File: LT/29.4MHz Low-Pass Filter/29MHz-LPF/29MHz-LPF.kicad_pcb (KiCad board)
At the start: 2 copper layers, 71.8 x 19.7 mm, 12 parts, among them J1 Conn_Coaxial, J2 Conn_Coaxial

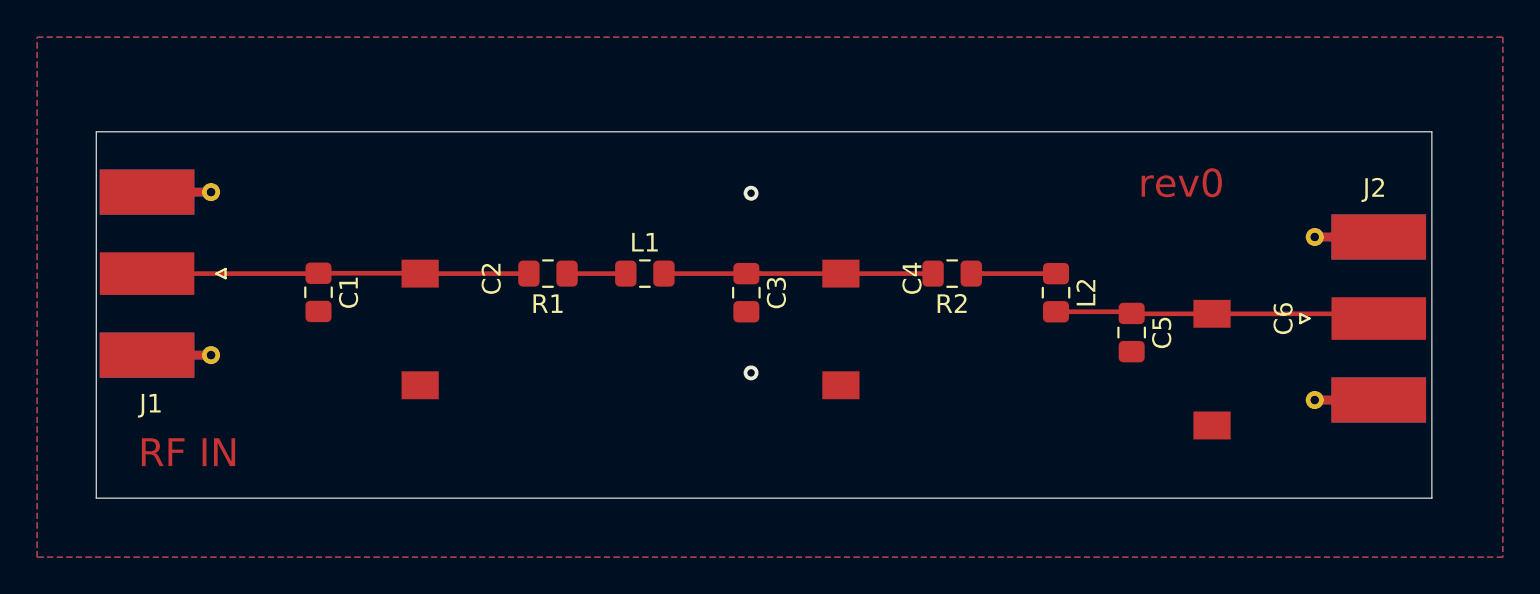
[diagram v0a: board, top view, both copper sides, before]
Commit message: removed 0 ohm resistors on 29.4MHz LPF
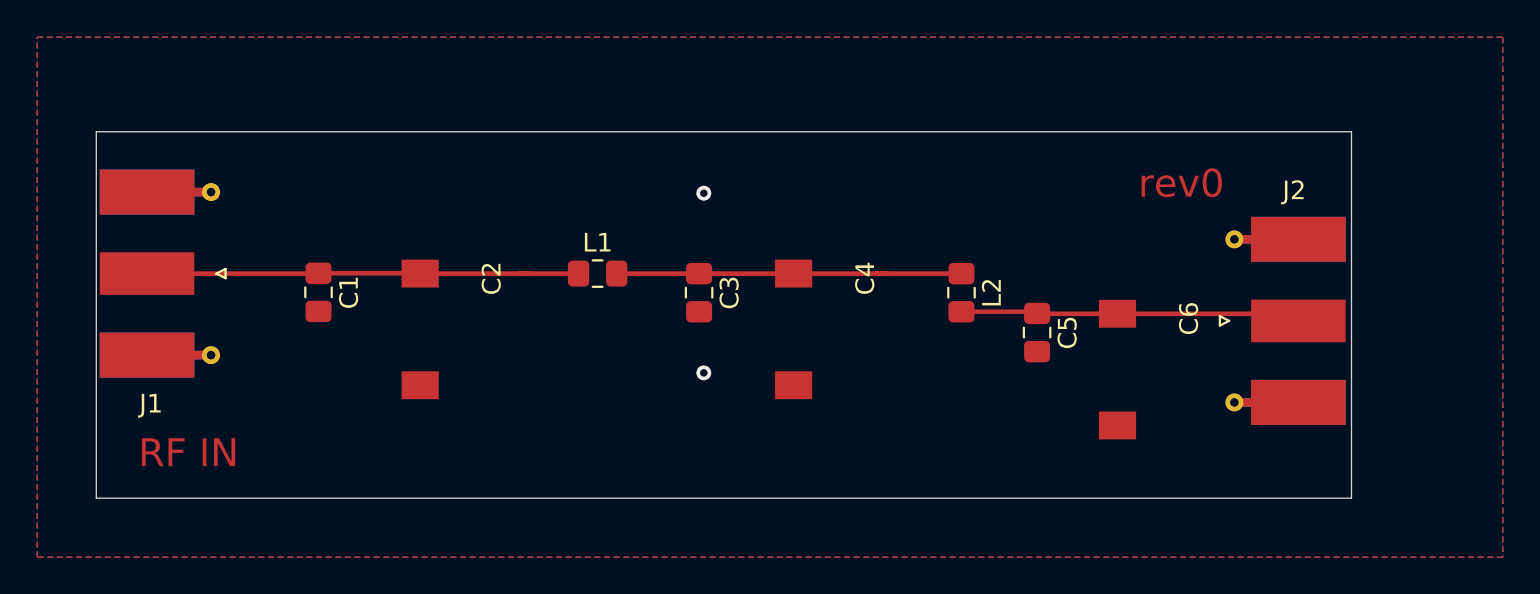
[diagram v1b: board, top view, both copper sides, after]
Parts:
- removed R1, R2: 0, Resistor_SMD:R_0805_2012Metric_Pad1.15x1.40mm_HandSolder
- moved C5 5.08 mm to (155.3, 92.1)
- moved C6 5.08 mm to (159.6, 91.1)
- moved L2 5.08 mm to (151.3, 89.9)
- moved J2 4.32 mm to (167.6, 91.4)
- moved C3 2.54 mm to (137.2, 89.9)
- moved C4 2.54 mm to (142.2, 88.9)
- moved L1 2.54 mm to (131.7, 88.9)
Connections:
- L1 pad 1: Net-(L1-Pad1) -> Net-(C1-Pad1)
- L2 pad 1: Net-(L2-Pad1) -> Net-(C3-Pad1)
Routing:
- net Net-(L2-Pad1): track 4.55 -> 0.00 mm
- net Net-(C3-Pad1): track 14.5 -> 19.0 mm
- net Net-(L1-Pad1): track 3.16 -> 0.00 mm
- net Net-(C1-Pad1): track 20.5 -> 23.7 mm
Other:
- board size 71.8 x 19.7 mm -> 67.4 x 19.7 mm
